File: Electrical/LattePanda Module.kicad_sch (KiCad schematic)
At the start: 10 parts, among them J12 Conn_01x03_Pin

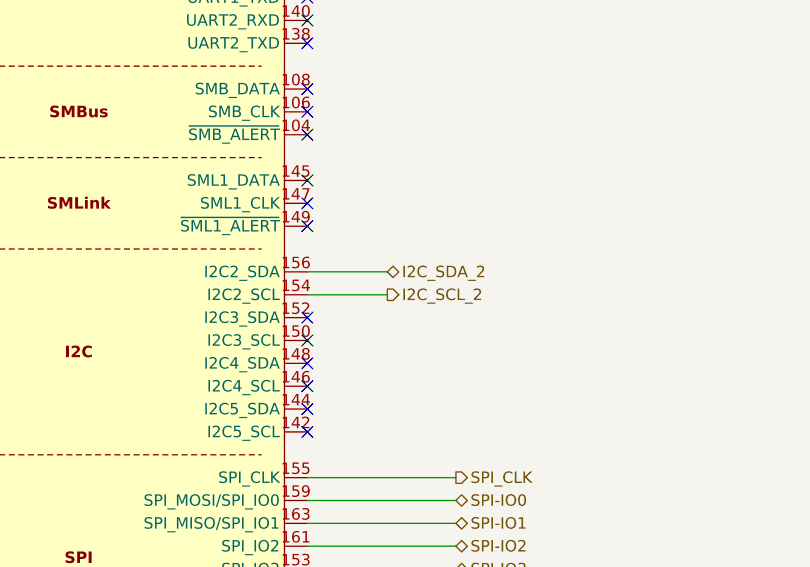
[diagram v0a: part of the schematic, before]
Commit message: switch to 20V PD input
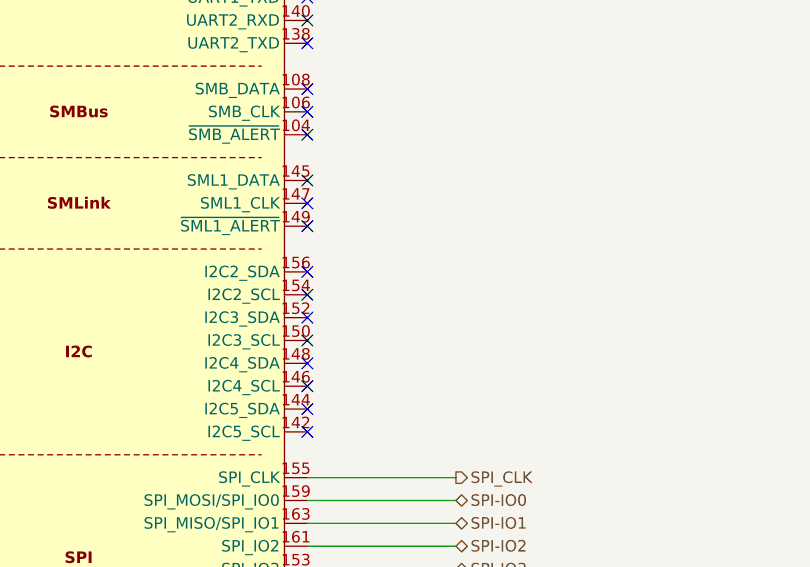
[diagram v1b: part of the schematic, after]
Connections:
- net I2C_SCL_2: no longer names the net of A1.154 (I2C2_SCL)
- net I2C_SDA_2: no longer names the net of A1.156 (I2C2_SDA)
- no-connect marks 91 -> 93
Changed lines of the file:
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@@
+	)
+	(no_connect
+		(at 351.79 218.44)
 	)
 	(no_connect
@@
 	)
 	(no_connect
+		(at 351.79 215.9)
+	)
+	(no_connect
 		(at 270.51 269.24)
 	)
@@
 	(wire
 		(pts
-			(xy 351.79 218.44) (xy 360.68 218.44)
-		)
-		(stroke
-			(width 0)
-			(type default)
-		)
-	)
-	(wire
-		(pts
 			(xy 373.38 274.32) (xy 373.38 276.86)
 		)
@@
 		(pts
 			(xy 238.76 212.09) (xy 270.51 212.09)
-		)
-		(stroke
-			(width 0)
-			(type default)
-		)
-	)
-	(wire
-		(pts
-			(xy 351.79 215.9) (xy 360.68 215.9)
 		)
 		(stroke
@@
 		)
 	)
-	(hierarchical_label "I2C_SDA_2"
-		(shape bidirectional)
-		(at 360.68 215.9 0)
-		(effects
-			(font
-				(size 1.27 1.27)
-			)
-			(justify left)
-		)
-	)
 	(hierarchical_label "SPI_CLK"
 		(shape output)
@@
 		(effects
 			(font
-				(size 1.27 1.27)
-			)
-			(justify left)
-		)
-	)
-	(hierarchical_label "I2C_SCL_2"
-		(shape output)
-		(at 360.68 218.44 0)
-		(effects
-			(font

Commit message: Major Overhaul
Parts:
- removed BT1: Battery_Cell, A_HDJ_Library:Battery_Holder_CR1220_S8411-45R, symbol Device:Battery_Cell
- added J17: 53261-0271, 532610271, symbol molex:53261-0271
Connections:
- net GND: now also J17.2, J17.MP1, J17.MP2
- net at R1.2: now also J17.1

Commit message: further changes required by DFA review
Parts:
- A1: footprint Module_LattePanda:LattePanda_Module_H8.0mm_Horizontal -> ddr slot:CONN260_2309413-1_TEC
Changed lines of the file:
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@@
 			)
 		)
-		(property "Footprint" "Module_LattePanda:LattePanda_Module_H8.0mm_Horizontal"
+		(property "Footprint" "ddr slot:CONN260_2309413-1_TEC"
 			(at 311.15 180.34 0)
 			(hide yes)
